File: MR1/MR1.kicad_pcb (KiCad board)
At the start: 2 copper layers, 14 parts, among them J1 Conn_01x04_Male, J2 Conn_01x04_Male, J3 Conn_01x04_Male, J4 Conn_01x04_Male, J5 Conn_01x02_Male, Q1 2SC1815, U5 LPC1768, U6 MPU6050, U7 R3008SB, U8 MCP2561-E-P

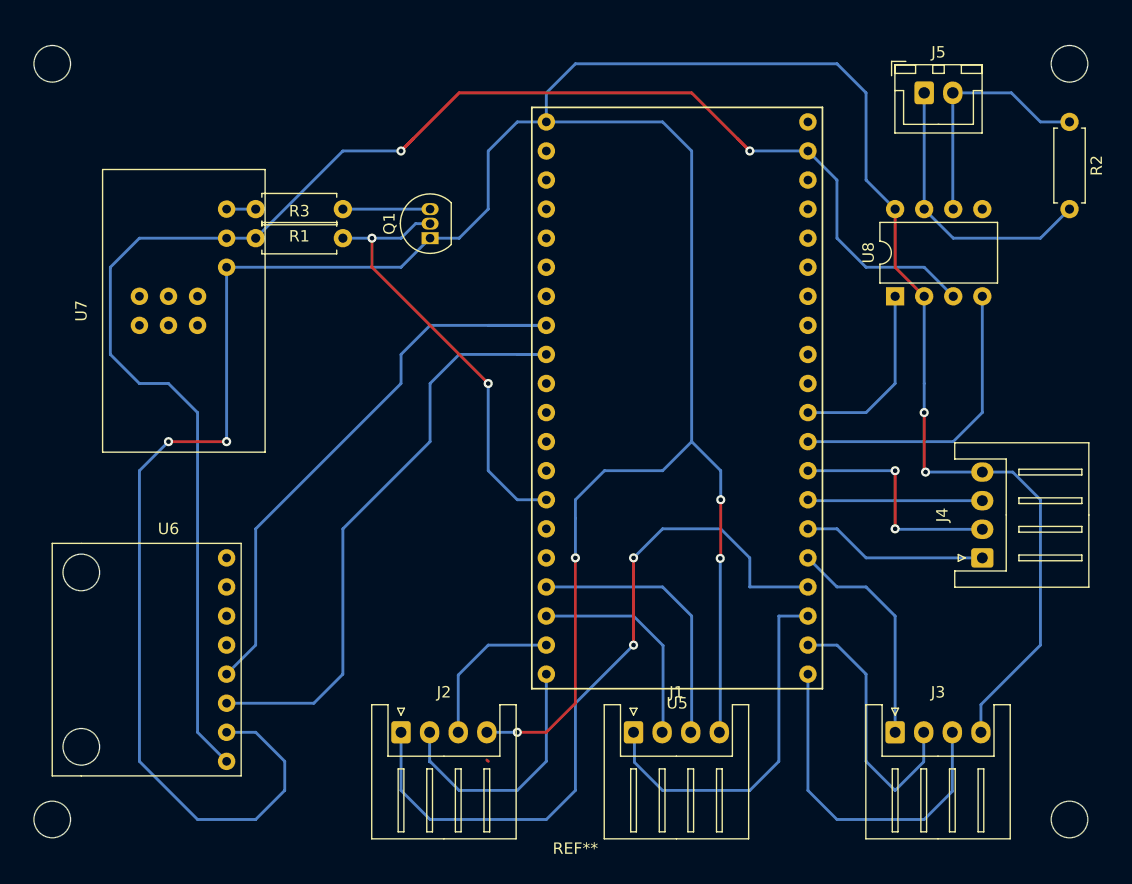
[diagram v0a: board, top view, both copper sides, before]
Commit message: update:MR1の基板完成
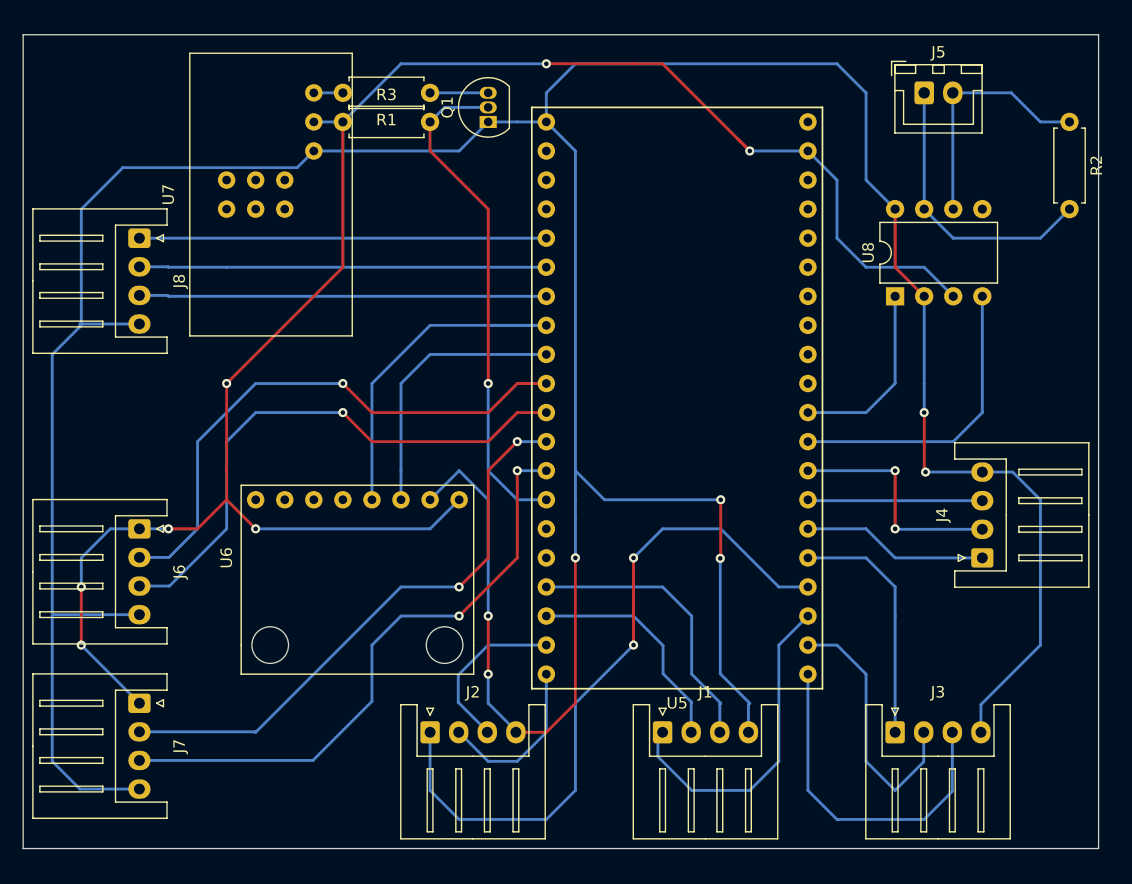
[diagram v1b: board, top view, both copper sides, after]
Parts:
- removed REF**: universal_B, MyFootprint:universal_B
- added J6: Conn_01x04_Male, Connector_JST:JST_XH_S4B-XH-A_1x04_P2.50mm_Horizontal, F.Cu at (106.7, 106.7)
- added J7: Conn_01x04_Male, Connector_JST:JST_XH_S4B-XH-A_1x04_P2.50mm_Horizontal, F.Cu at (106.7, 121.9)
- added J8: Conn_01x04_Male, Connector_JST:JST_XH_S4B-XH-A_1x04_P2.50mm_Horizontal, F.Cu at (106.7, 81.3)
- moved U6 17.0 mm to (124.5, 109.2), turned to 270 degrees
- moved R1 12.7 mm to (132.1, 68.6)
- moved R3 12.7 mm to (124.5, 71.1)
- moved U7 12.7 mm to (119.4, 77.5)
- moved Q1 11.4 mm to (137.2, 71.1)
- moved J2 2.54 mm to (132.1, 124.5)
- moved J1 2.54 mm to (152.4, 124.5)
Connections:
- U5 pad 10: Net-(U5-Pad10) -> enc_X_b
- U5 pad 11: Net-(U5-Pad11) -> enc_X_a
- U5 pad 12: Net-(U5-Pad12) -> enc_Y_b
- U5 pad 13: Net-(U5-Pad13) -> enc_Y_a
- U5 pad 5: Net-(U5-Pad5) -> led_Red
- U5 pad 6: Net-(U5-Pad6) -> led_Green
- U5 pad 7: Net-(U5-Pad7) -> led_Blue
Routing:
- net enc_Y_a: track 0.00 -> 53.4 mm, vias 0 -> 2
- net enc_Y_b: track 0.00 -> 50.6 mm, vias 0 -> 2
- net enc_X_b: track 0.00 -> 48.4 mm, vias 0 -> 2
- net enc_X_a: track 0.00 -> 48.4 mm, vias 0 -> 2
- net led_Blue: track 0.00 -> 35.6 mm
- net led_Green: track 0.00 -> 35.6 mm
- net led_Red: track 0.00 -> 35.6 mm
- net I2C_scl: track 53.5 -> 23.9 mm
- net GND: track 316.0 -> 337.8 mm, vias 11 -> 10
- net I2C_sda: track 53.1 -> 32.6 mm
- net +5V: track 142.3 -> 160.2 mm, vias 2 -> 7
- net IO_2B: track 22.5 -> 14.7 mm
- net Serial_rx: track 38.4 -> 44.3 mm, vias 2 -> 1
- net PWM_2: track 64.7 -> 60.7 mm
- net PWM_1: track 32.6 -> 28.7 mm
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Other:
- board outline added: 94 x 71.1 mm

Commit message: update:XHを変更
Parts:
- J6: footprint Connector_JST:JST_XH_S4B-XH-A_1x04_P2.50mm_Horizontal -> Connector_JST:JST_XH_B4B-XH-AM_1x04_P2.50mm_Vertical
- J7: footprint Connector_JST:JST_XH_S4B-XH-A_1x04_P2.50mm_Horizontal -> Connector_JST:JST_XH_B4B-XH-A_1x04_P2.50mm_Vertical

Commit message: fix: MR1
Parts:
- added REF**: universal_B, MyFootprint:universal_B, F.Cu at (142.2, 99.1)
- J6: footprint Connector_JST:JST_XH_B4B-XH-AM_1x04_P2.50mm_Vertical -> Connector_JST:JST_XH_S4B-XH-A_1x04_P2.50mm_Horizontal
- J7: footprint Connector_JST:JST_XH_B4B-XH-A_1x04_P2.50mm_Vertical -> Connector_JST:JST_XH_S4B-XH-A_1x04_P2.50mm_Horizontal
- moved R3 43.3 mm to (152.4, 104.1), turned to 180 degrees
- moved Q1 30.7 mm to (149.9, 99.1), turned to 180 degrees
- moved R1 21.8 mm to (144.8, 86.4), turned to 0 degrees
- moved J7 7.62 mm to (106.7, 114.3)
- moved J2 7.62 mm to (139.7, 124.5)
- moved J6 7.50 mm to (106.7, 99.2)
- moved U7 7.41 mm to (125.7, 73.7), turned to 0 degrees
- moved U6 5.08 mm to (124.5, 104.1)
- moved J1 5.08 mm to (157.5, 124.5)
- moved J8 2.66 mm to (106.7, 83.9)
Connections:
- U5 pad 10: enc_X_b -> I2C_scl
- U5 pad 11: enc_X_a -> enc_X_b
- U5 pad 12: enc_Y_b -> enc_X_a
- U5 pad 13: enc_Y_a -> Net-(U5-Pad13)
- U5 pad 15: Net-(U5-Pad15) -> enc_Y_b
- U5 pad 16: Net-(U5-Pad16) -> enc_Y_a
- U5 pad 8: I2C_sda -> Net-(U5-Pad8)
- U5 pad 9: I2C_scl -> I2C_sda
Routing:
- net GND: track 337.8 -> 431.8 mm
- net Net-(R1-Pad2): track 2.54 -> 43.4 mm
- net +5V: track 160.2 -> 200.6 mm, vias 7 -> 8
- net Serial_rx: track 44.3 -> 9.20 mm, vias 1 -> 0
- net PWM_2: track 60.7 -> 37.2 mm
- net PWM_1: track 28.7 -> 14.8 mm, vias 0 -> 2
- net enc_Y_a: track 53.4 -> 39.8 mm, vias 2 -> 0
- net I2C_sda: track 32.6 -> 19.9 mm
- net enc_Y_b: track 50.6 -> 39.8 mm, vias 2 -> 0
- net enc_X_a: track 48.4 -> 37.7 mm, vias 2 -> 0
- net enc_X_b: track 48.4 -> 37.7 mm, vias 2 -> 0
- net Net-(Q1-Pad3): track 5.08 -> 15.2 mm
- net IO_2B: track 14.7 -> 5.10 mm
- net I2C_scl: track 23.9 -> 16.3 mm
- net IO_3A: track 30.0 -> 22.5 mm
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
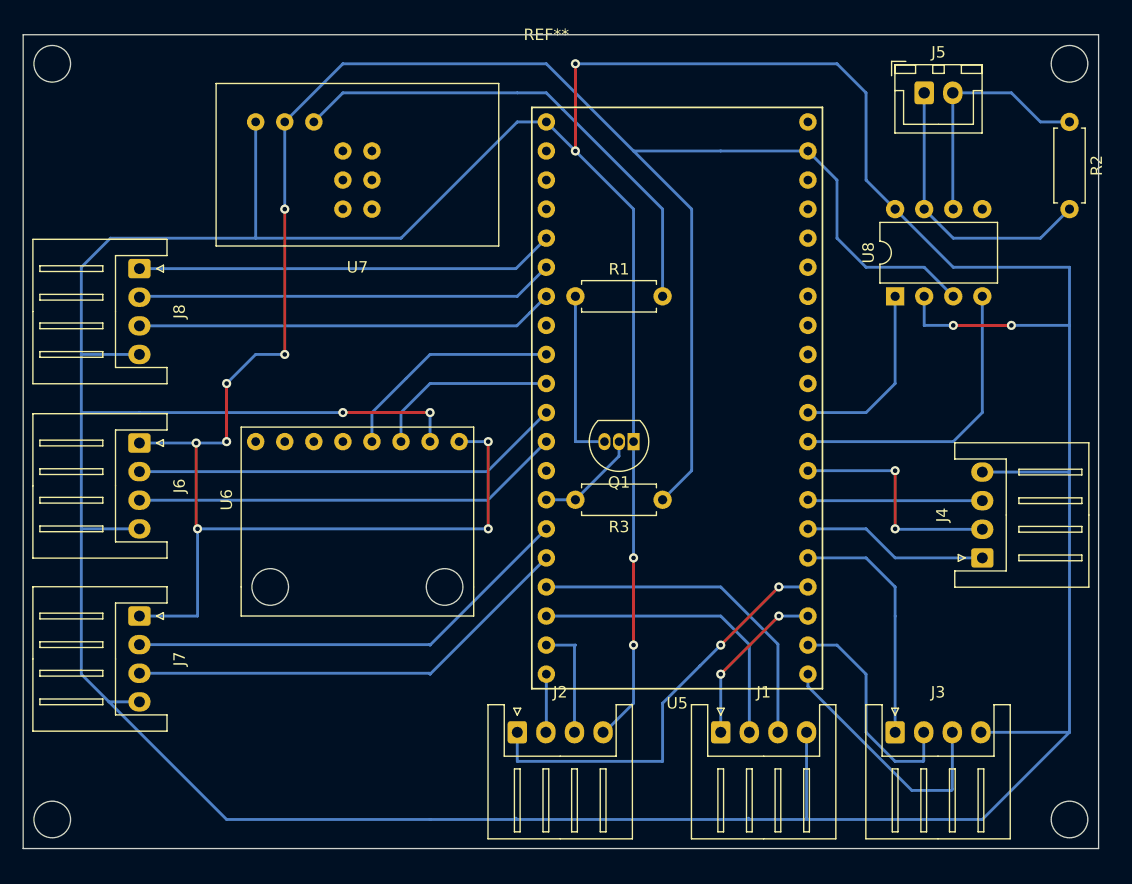
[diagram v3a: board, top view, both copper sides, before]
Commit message: update:設計変更に伴う改修、CAN通信周りの不具合を修正
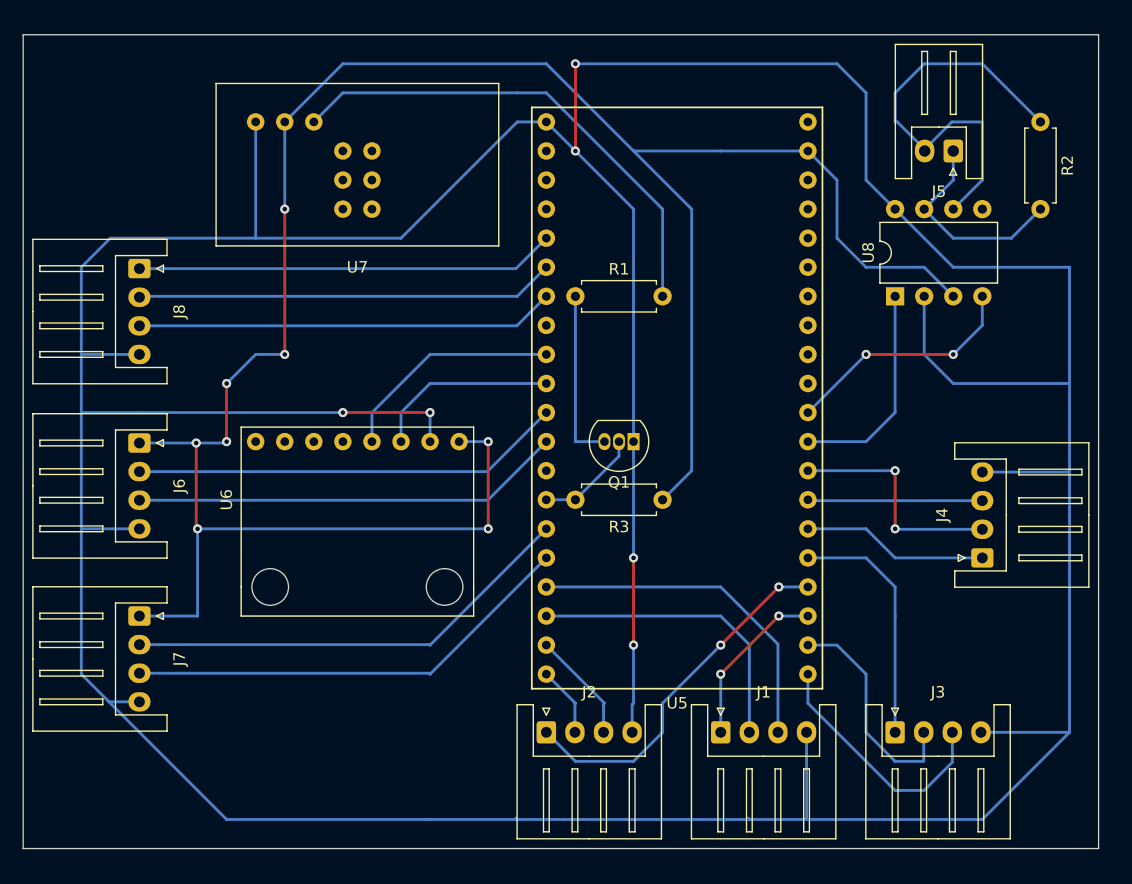
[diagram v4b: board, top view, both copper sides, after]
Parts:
- removed REF**: universal_B, MyFootprint:universal_B
- J5: footprint Connector_JST:JST_XH_B2B-XH-A_1x02_P2.50mm_Vertical -> Connector_JST:JST_XH_S2B-XH-A_1x02_P2.50mm_Horizontal
- moved J5 5.68 mm to (177.8, 73.7), turned to 180 degrees
- moved J2 2.54 mm to (142.2, 124.5)
- moved R2 2.54 mm to (185.4, 71.1)
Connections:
- U5 pad 29: CAN_rd -> CAN_td
- U5 pad 30: CAN_td -> CAN_rd
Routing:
- net CAN_L: track 21.4 -> 36.9 mm
- net CAN_H: track 25.0 -> 18.4 mm
- net CAN_rd: track 26.5 -> 20.9 mm, vias 0 -> 2
- net PWM_2: track 37.2 -> 31.8 mm
- net CAN_td: track 16.3 -> 18.8 mm
- net GND: track 431.8 -> 434.3 mm, vias 10 -> 8
- net IO_2B: track 5.10 -> 6.15 mm
- net IO_2A: track 10.2 -> 9.47 mm
- net IO_3A: track 22.5 -> 22.0 mm

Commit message: update : mr1:sub_swの追加   mr2:エンコーダーの増設
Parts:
- added J10: Conn_01x02_Male, Connector_JST:JST_XH_S2B-XH-A_1x02_P2.50mm_Horizontal, F.Cu at (132.1, 124.5)
- added J9: Conn_01x02_Male, Connector_JST:JST_XH_S2B-XH-A_1x02_P2.50mm_Horizontal, F.Cu at (121.9, 124.5)
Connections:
- U5 pad 13: Net-(U5-Pad13) -> sub_sw2
- U5 pad 8: Net-(U5-Pad8) -> sub_sw
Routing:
- net sub_sw: track 0.00 -> 58.6 mm, vias 0 -> 2
- net sub_sw2: track 0.00 -> 28.6 mm, vias 0 -> 2
- net GND: track 434.3 -> 449.6 mm
- net enc_X_a: track 37.7 -> 39.8 mm
- net enc_X_b: track 37.7 -> 39.7 mm
- net +5V: track 200.6 -> 199.1 mm
